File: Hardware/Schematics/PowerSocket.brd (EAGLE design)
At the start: 100 x 80 mm, 73 parts, among them T1 BT138-H, T2 BT138-H, T3 BT138-H, T4 BT138-H, T5 BT138-H, T6 BT138-H

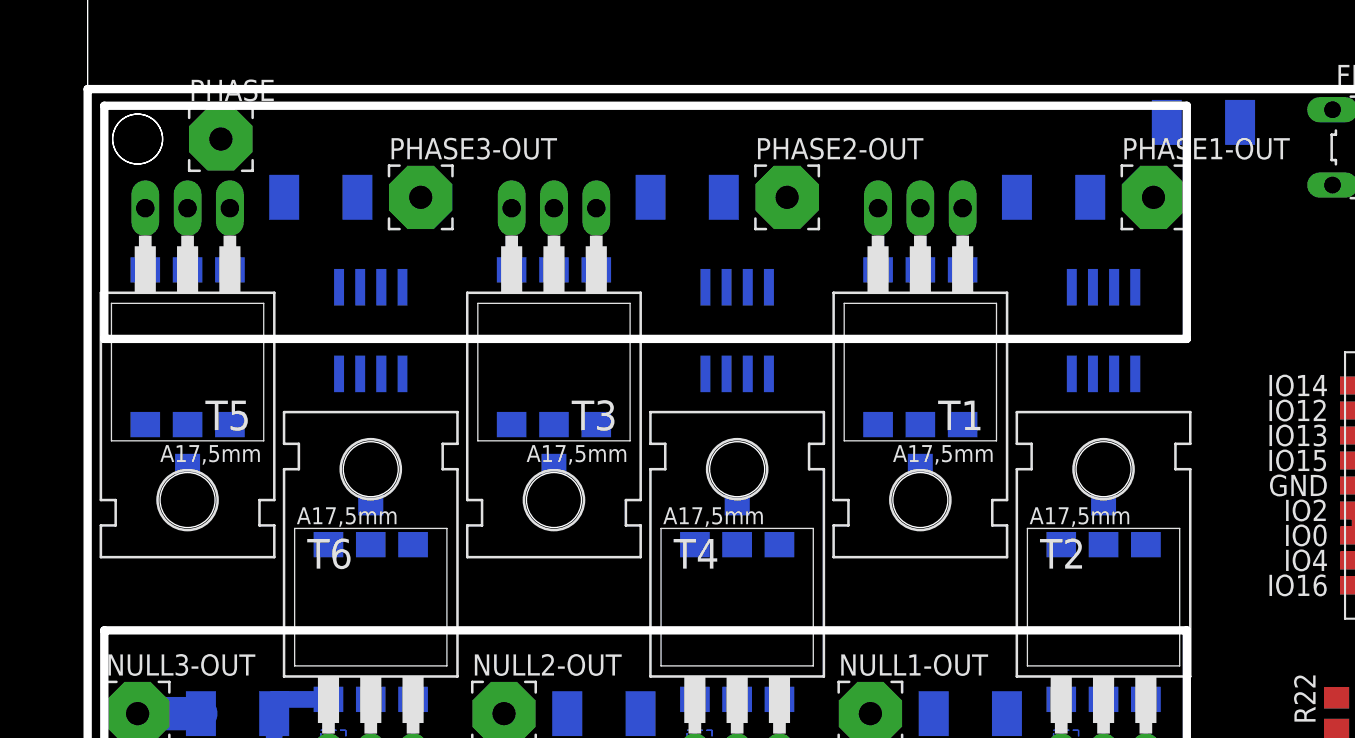
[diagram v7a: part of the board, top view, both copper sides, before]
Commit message: Changed package for triac.
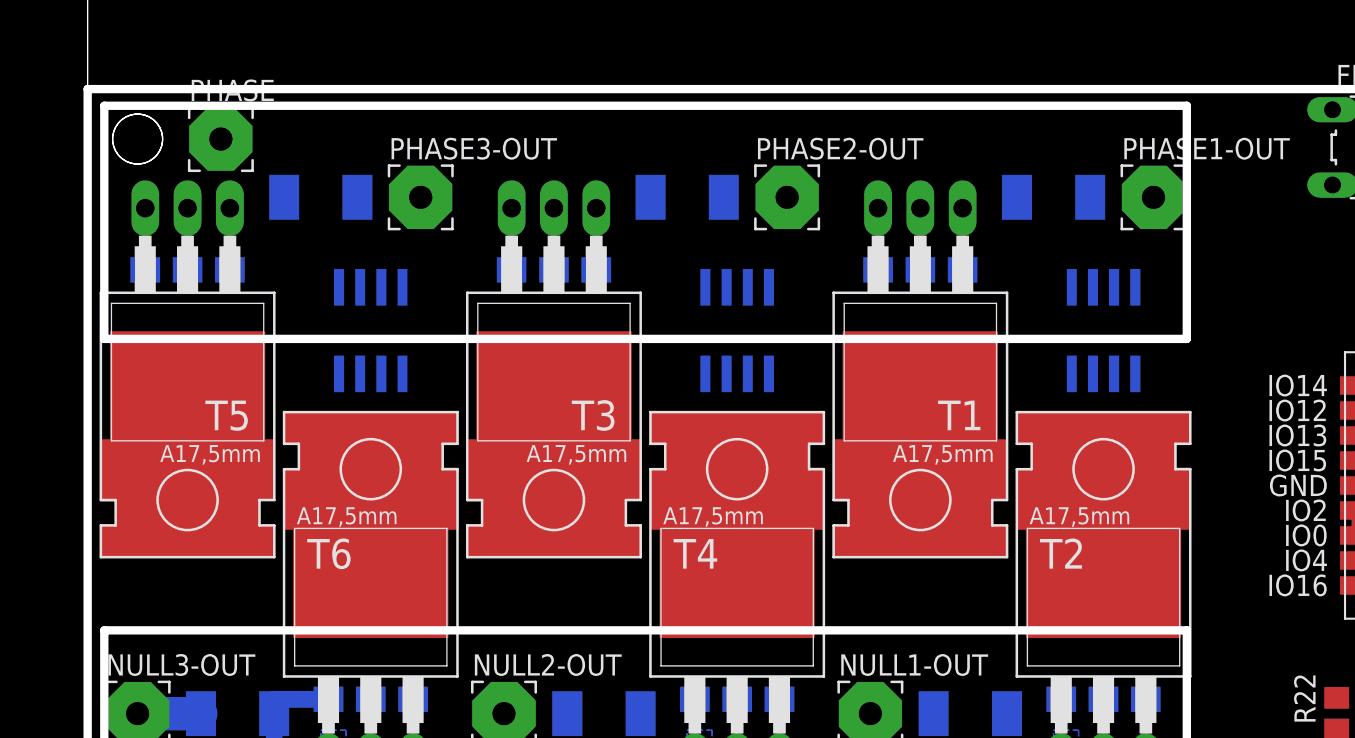
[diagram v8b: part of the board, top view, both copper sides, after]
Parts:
- removed R24: 0, eagle-ltspice:R2010
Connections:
- removed net N$41: D1.C, R24.1
- net PHASE: now also D1.C; no longer R24.2
